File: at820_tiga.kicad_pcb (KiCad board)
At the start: 2 copper layers, 98 x 88.5 mm, 102 parts, among them J1 SWD, J10 QSPI_SWITCH, J11 Conn_01x03_Pin, J12 Conn_01x03_Pin, J13 TEST_MODE, J2 download, J3 I2C, J4 uart0, J5 SPI0, J6 power, J7 Conn_01x04_Pin, J8 USB_C_Receptacle_USB2.0_16P, J9 USB_C_Receptacle_USB2.0_16P, SW1 OS102011MS2QN1, SW2 Wakeup Button, SW3 Reset Button, SW4 MY_SW_DPST, SW6 Boot Button, U2 CH343P, U3 TS5A23157DGS, U4 AMS1117-3.3, U5 MIX2909, Y1 Crystal_GND24

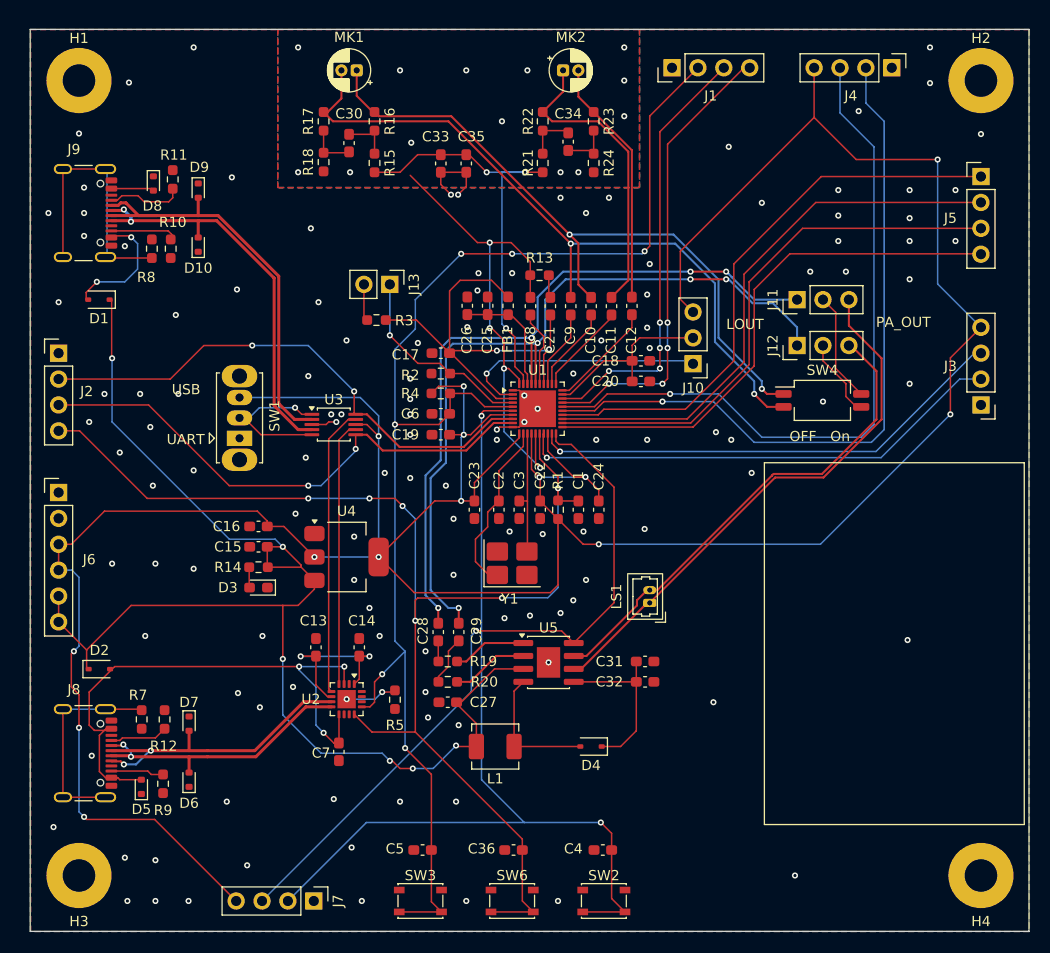
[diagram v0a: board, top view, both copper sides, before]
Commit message: modify board egde
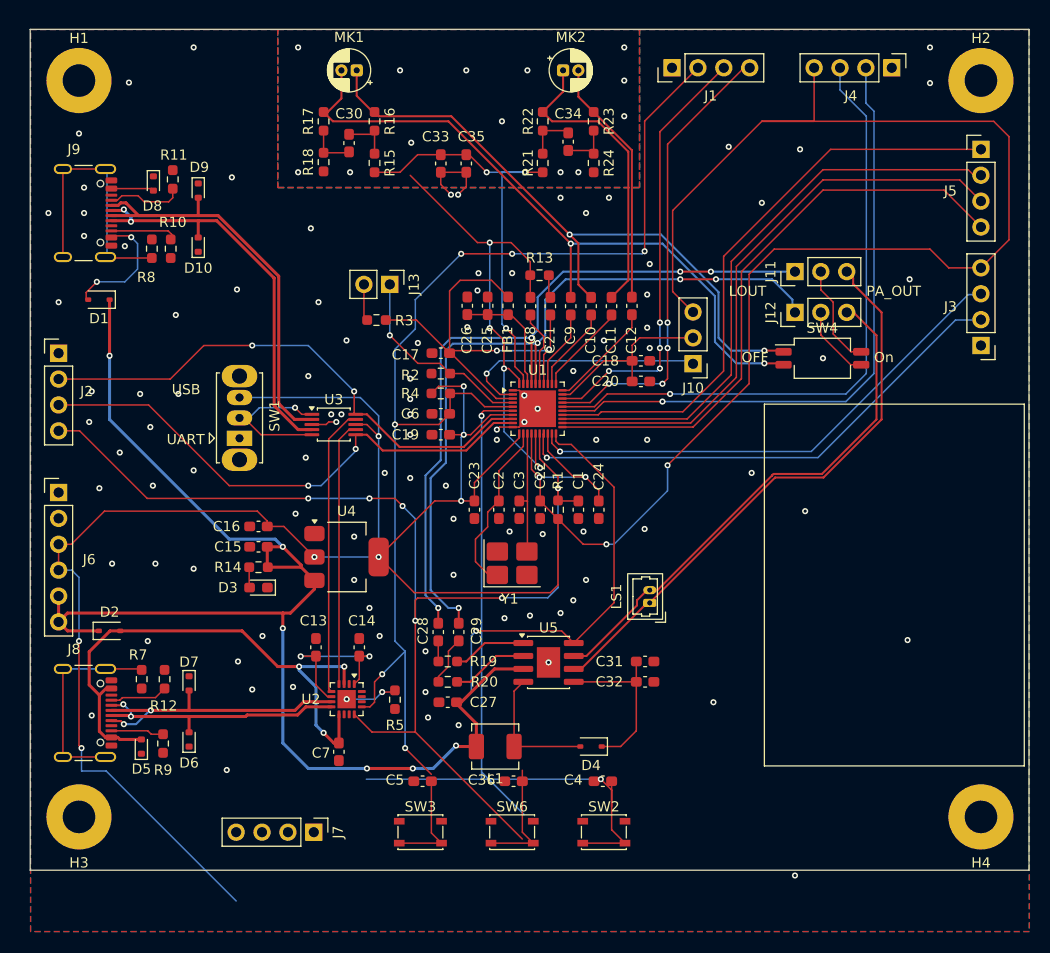
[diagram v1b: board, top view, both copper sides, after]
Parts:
- moved C36 6.75 mm to (141.1, 129.8)
- moved C4 6.75 mm to (149.9, 129.8)
- moved C5 6.75 mm to (132.2, 129.8)
- moved J7 6.75 mm to (121.5, 134.8)
- moved SW2 6.75 mm to (150.0, 134.8)
- moved SW3 6.75 mm to (132.0, 134.8)
- moved SW6 6.75 mm to (141.0, 134.8)
- moved J3 5.83 mm to (187.0, 87.0)
- moved H3 5.75 mm to (98.5, 133.2)
- moved H4 5.75 mm to (187.0, 133.2)
- moved SW4 4.14 mm to (171.4, 88.2)
- moved D5 3.95 mm to (104.6, 126.3)
- moved J8 3.95 mm to (98.0, 123.0)
- moved R12 3.95 mm to (106.9, 119.7)
- moved R7 3.95 mm to (104.7, 119.7)
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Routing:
- net /AT_PWM0: track 70.5 -> 41.5 mm
- net +3V3: track 366.7 -> 382.5 mm, vias 16 -> 14
- net /AT_GPIO3: track 92.9 -> 82.0 mm
- net /AT_UART0_RXD: track 70.4 -> 62.4 mm
- net /AT_UART0_TXD: track 69.7 -> 62.2 mm
- net /AT_RST: track 134.2 -> 126.8 mm
- net /AT_SPI0_CS0: track 52.5 -> 58.3 mm
- net /AT_SPI0_MI: track 53.7 -> 58.1 mm
- net /audio/PA_OUTN: track 48.1 -> 51.7 mm
- net /AT_RMIC_N: track 71.5 -> 68.4 mm
- net /AT_RMIC_P: track 67.3 -> 64.5 mm
- net /audio/PA_OUTP: track 53.4 -> 56.3 mm
- net /AT_I2C0_SDA: track 48.3 -> 50.7 mm
- net /AT_I2C0_SCL: track 47.4 -> 49.8 mm
- net /AT_SPI0_MO: track 54.9 -> 57.2 mm
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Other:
- board size 98 x 88.5 mm -> 98 x 82.5 mm

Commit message: pcb dev
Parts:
- moved C36 1.25 mm to (141.1, 131.0)
- moved C4 1.25 mm to (149.9, 131.0)
- moved C5 1.25 mm to (132.2, 131.0)
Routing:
- net /AT_PWM0: track 41.5 -> 67.7 mm
- net /AT_BOOT: track 128.4 -> 124.2 mm
- net +3V3: track 382.5 -> 379.0 mm
- net /AT_GPIO3: track 82.0 -> 85.4 mm
- net /AT_RST: track 126.8 -> 127.5 mm

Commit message: beta 2, modify board size, add some silkscreen
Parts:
- added D1: LED, LED_SMD:LED_0603_1608Metric_Pad1.05x0.95mm_HandSolder, F.Cu at (126.2, 98.0)
- added D2: LED, LED_SMD:LED_0603_1608Metric_Pad1.05x0.95mm_HandSolder, F.Cu at (120.4, 98.0)
- added R4: 2K, Resistor_SMD:R_0603_1608Metric_Pad0.98x0.95mm_HandSolder, F.Cu at (126.2, 99.9)
- added R5: 2K, Resistor_SMD:R_0603_1608Metric_Pad0.98x0.95mm_HandSolder, F.Cu at (120.4, 99.9)
- J10: renamed from J9; value USB_C_Receptacle_USB2.0_16P -> USB
- J3: renamed from J2; value download -> Download
- J4: renamed from J3; value I2C -> I2C0
- J5: renamed from J4; value uart0 -> UART0
- J7: renamed from J6; value power -> Power
- J9: renamed from J8; value USB_C_Receptacle_USB2.0_16P -> UART
- L1: value 6.8uH -> 6.8uH PCR0420-6R8-M; footprint Inductor_SMD:L_Sunlord_MWSA0402S -> Inductor_SMD:L_Changjiang_FTC404020S
- SW2: renamed from SW3; value Reset Button -> Reset
- SW3: renamed from SW2; value Wakeup Button -> Wakeup
- SW4: renamed from SW6; value Boot Button -> Boot
- SW5: renamed from SW4; value MY_SW_DPST -> Loopback
- moved J5 5.77 mm to (172.5, 59.2)
- moved H3 5.00 mm to (182.0, 61.0)
- moved H4 5.00 mm to (182.0, 133.2)
- moved J2 4.72 mm to (152.0, 59.2)
- moved J6 2.54 mm to (184.5, 67.3)
- moved J4 2.50 mm to (184.5, 87.0)
- moved MK2 2.50 mm to (143.5, 60.0)
- moved C35 2.25 mm to (144.2, 67.0)
- moved R22 2.25 mm to (141.8, 69.1)
- moved R23 2.25 mm to (141.8, 65.0)
- moved R24 2.25 mm to (146.8, 65.0)
- moved R25 2.25 mm to (146.8, 69.1)
- moved C34 1.75 mm to (132.2, 69.1)
- moved C36 1.75 mm to (134.8, 69.1)
- moved D6 1.18 mm to (105.8, 126.3)
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- renumbered C13 to C10, C14 to C11, C5 to C12, C6 to C13, C4 to C14, C36 to C15, C15 to C16, C16 to C17, C17 to C18, C18 to C19, C19 to C20, C20 to C21, C21 to C22, C22 to C23, C23 to C24, C24 to C25, C25 to C26, C26 to C27, C27 to C28, C28 to C29, C29 to C30, C30 to C31, C31 to C32, C32 to C33, C33 to C34, C34 to C35, C35 to C36, C7 to C4, C8 to C5, C9 to C6, C10 to C7, C11 to C8, C12 to C9, D1 to D10, D3 to D11, D4 to D12, D6 to D3, D9 to D4, D7 to D5, D5 to D6, D8 to D7, D10 to D8, D2 to D9, H3 to H2, H2 to H3, J13 to J1, J10 to J11, J11 to J12, J12 to J13, J1 to J2, J5 to J6, J7 to J8, R13 to R10, R9 to R11, R10 to R12, R12 to R13, R11 to R14, R14 to R15, R15 to R16, R16 to R17, R17 to R18, R18 to R19, R19 to R20, R20 to R21, R21 to R22, R22 to R23, R23 to R24, R24 to R25, R5 to R6, R4 to R7, R7 to R8, R8 to R9, U3 to U1, U1 to U2, U2 to U3
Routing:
- net VBUS: track 55.1 -> 73.4 mm, vias 3 -> 7
- net +3V3: track 379.0 -> 367.1 mm, vias 14 -> 17
- net GND: track 20.4 -> 31.3 mm, vias 102 -> 94
- net AT_MICBIAS: track 42.0 -> 37.3 mm
- net VBUS_B: track 16.4 -> 20.8 mm, vias 2 -> 3
- net /AT_UART0_RXD: track 62.4 -> 65.4 mm
- net /AT_UART0_TXD: track 62.2 -> 65.1 mm
- net /AT_SPI0_MI: track 58.1 -> 55.5 mm
- net /AT_SPI0_CS0: track 58.3 -> 55.8 mm
- net /CH_UART_RXD: track 26.0 -> 28.4 mm
- net /AT_SPI0_CLK: track 58.4 -> 56.3 mm
- net /AT_SPI0_MO: track 57.2 -> 55.2 mm
- net /AT_I2C0_SDA: track 50.7 -> 48.8 mm
- net Net-(D1-A): track 0.00 -> 1.88 mm
- net Net-(D2-A): track 0.00 -> 1.87 mm
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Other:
- board size 98 x 82.5 mm -> 93.5 x 82.5 mm
- board text added: "1V8"
- board text added: "3V3"
- board text added: "5V"
- board text added: "BOOT"
- board text added: "CLK"
- board text added: "CS"
- board text added: "GND"
- board text added: "MI"
- board text added: "MO"
- board text added: "RST"
- board text added: "RX"
- board text added: "SCL"
- board text added: "SDA"
- board text added: "SWCLK"
- board text added: "SWDIO"
- board text added: "TX"

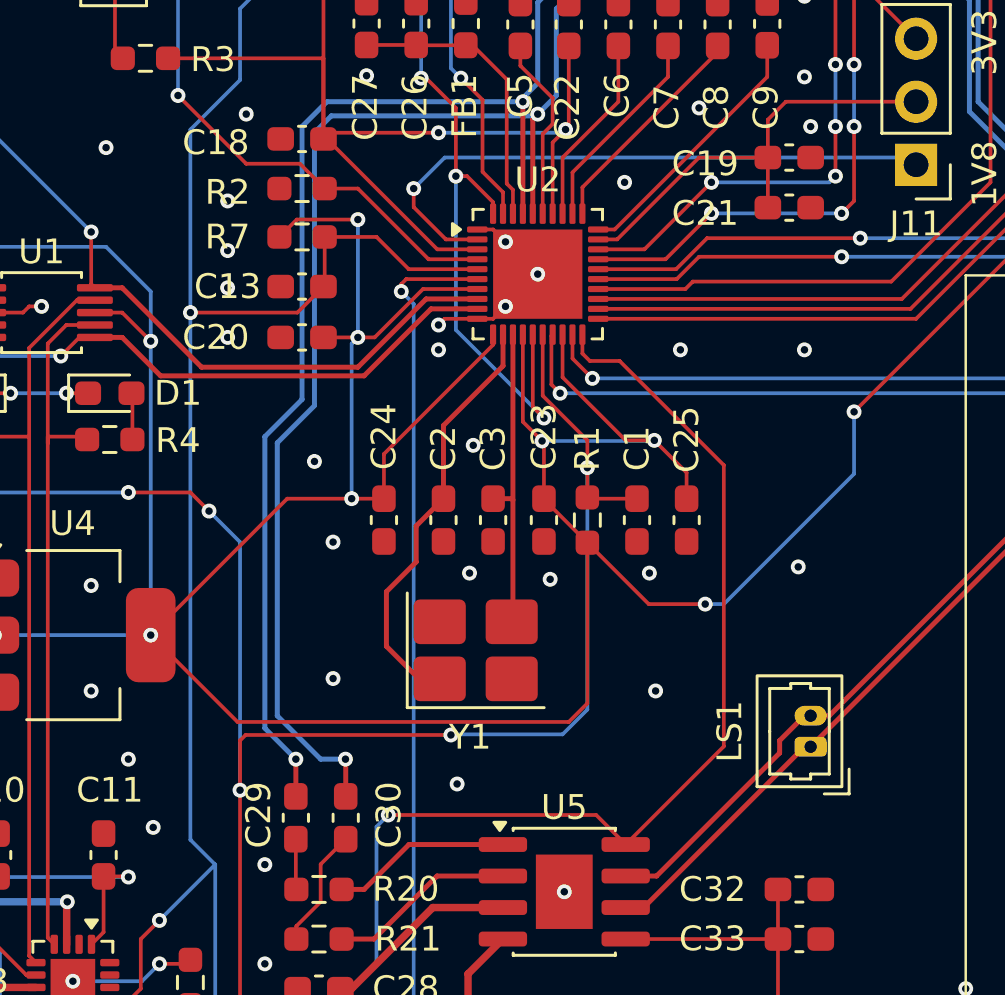
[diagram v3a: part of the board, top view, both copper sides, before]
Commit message: refactor crystal pcb
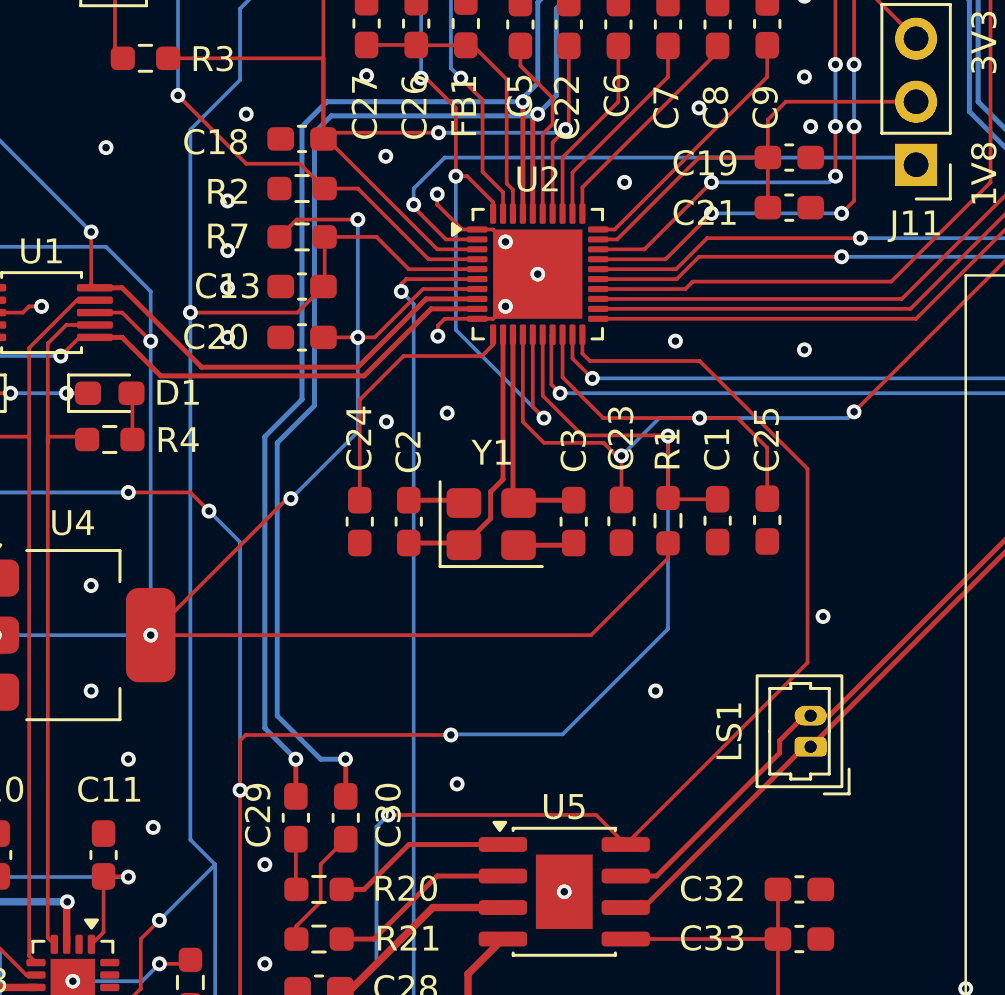
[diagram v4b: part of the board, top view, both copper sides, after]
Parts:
- Y1: footprint Crystal:Crystal_SMD_3225-4Pin_3.2x2.5mm_HandSoldering -> Crystal:Crystal_SMD_3225-4Pin_3.2x2.5mm
- moved Y1 5.13 mm to (141.6, 103.3)
- moved C3 3.25 mm to (144.9, 103.2)
- moved C1 3.25 mm to (150.8, 103.1)
- moved R1 3.25 mm to (148.8, 103.1)
- moved C25 3.25 mm to (152.8, 103.1)
- moved C23 3.13 mm to (146.9, 103.2)
- moved C2 1.40 mm to (138.3, 103.2), turned to 90 degrees
- moved C24 0.98 mm to (136.3, 103.2)
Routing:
- net +3V3: track 367.1 -> 357.0 mm, vias 17 -> 16
- net GND: track 31.3 -> 38.7 mm, vias 94 -> 90
- net /AT_BOOT: track 124.1 -> 130.2 mm
- net /AT_XT_IN: track 17.2 -> 11.4 mm
- net /AT_PWM0: track 67.7 -> 72.4 mm
- net /AT_XT_OUT: track 12.4 -> 9.15 mm

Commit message: add logo, fix all no connect bugs
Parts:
- added AT820-Tiga: LOGO, at820_tiga_pcb_lib:logo, F.Cu at (155.4, 72.5)
- MK1: value Microphone -> RMic
- MK2: value Microphone -> LMic
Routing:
- net GND: track 38.7 -> 49.8 mm, vias 90 -> 91
- net +3V3: track 357.0 -> 367.8 mm, vias 16 -> 20
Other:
- board text added: "GPIO3"
- board text added: "PWM0"
